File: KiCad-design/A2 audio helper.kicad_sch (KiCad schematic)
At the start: 35 parts, among them J1 PIN HEADER 1x2, J10 PIN HEADER 1x2, J11 PIN HEADER 1x3, J12 PIN HEADER 1x3, J13 PIN HEADER 1x3, J14 PIN HEADER 2x6, J2 PIN HEADER 1x2, J3 PIN HEADER 1x2, J4 SJ1-3515N, J5 PIN HEADER 1x3, J6 PIN HEADER 1x3, J7 SJ1-3515N, J8 PIN HEADER 1x5, J9 PIN HEADER 1x2, K1 SR11-5V-200-2C, SW2 SW_DPDT_x2, U1 pam8403

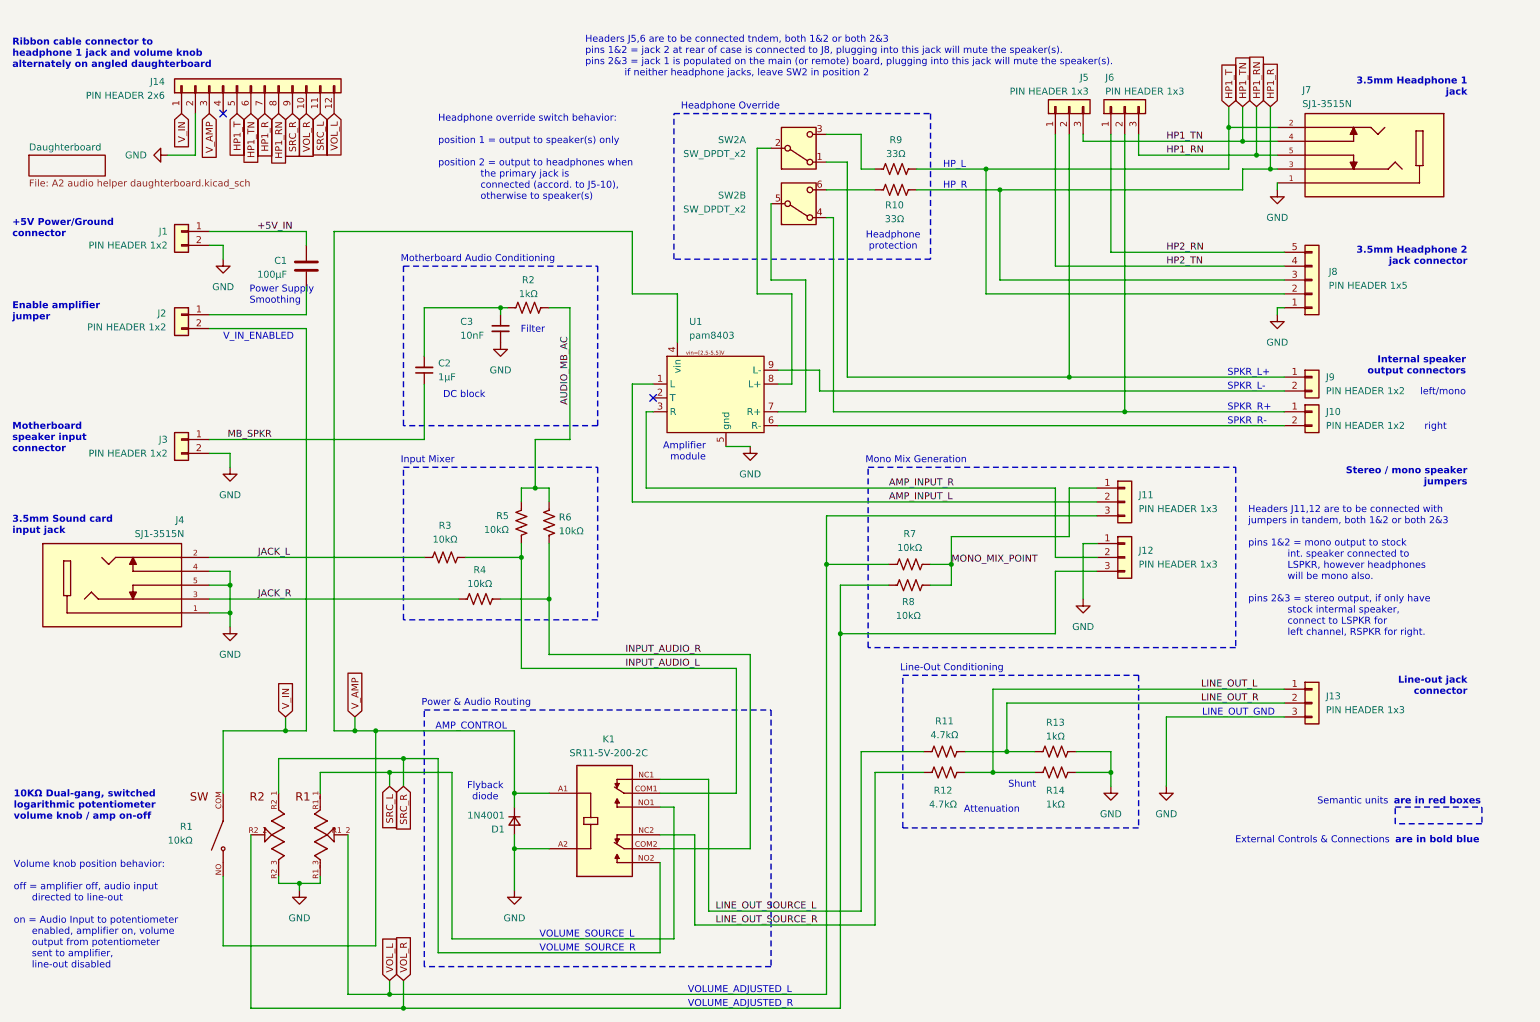
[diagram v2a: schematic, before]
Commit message: made power & speaker input connectors also horizontal
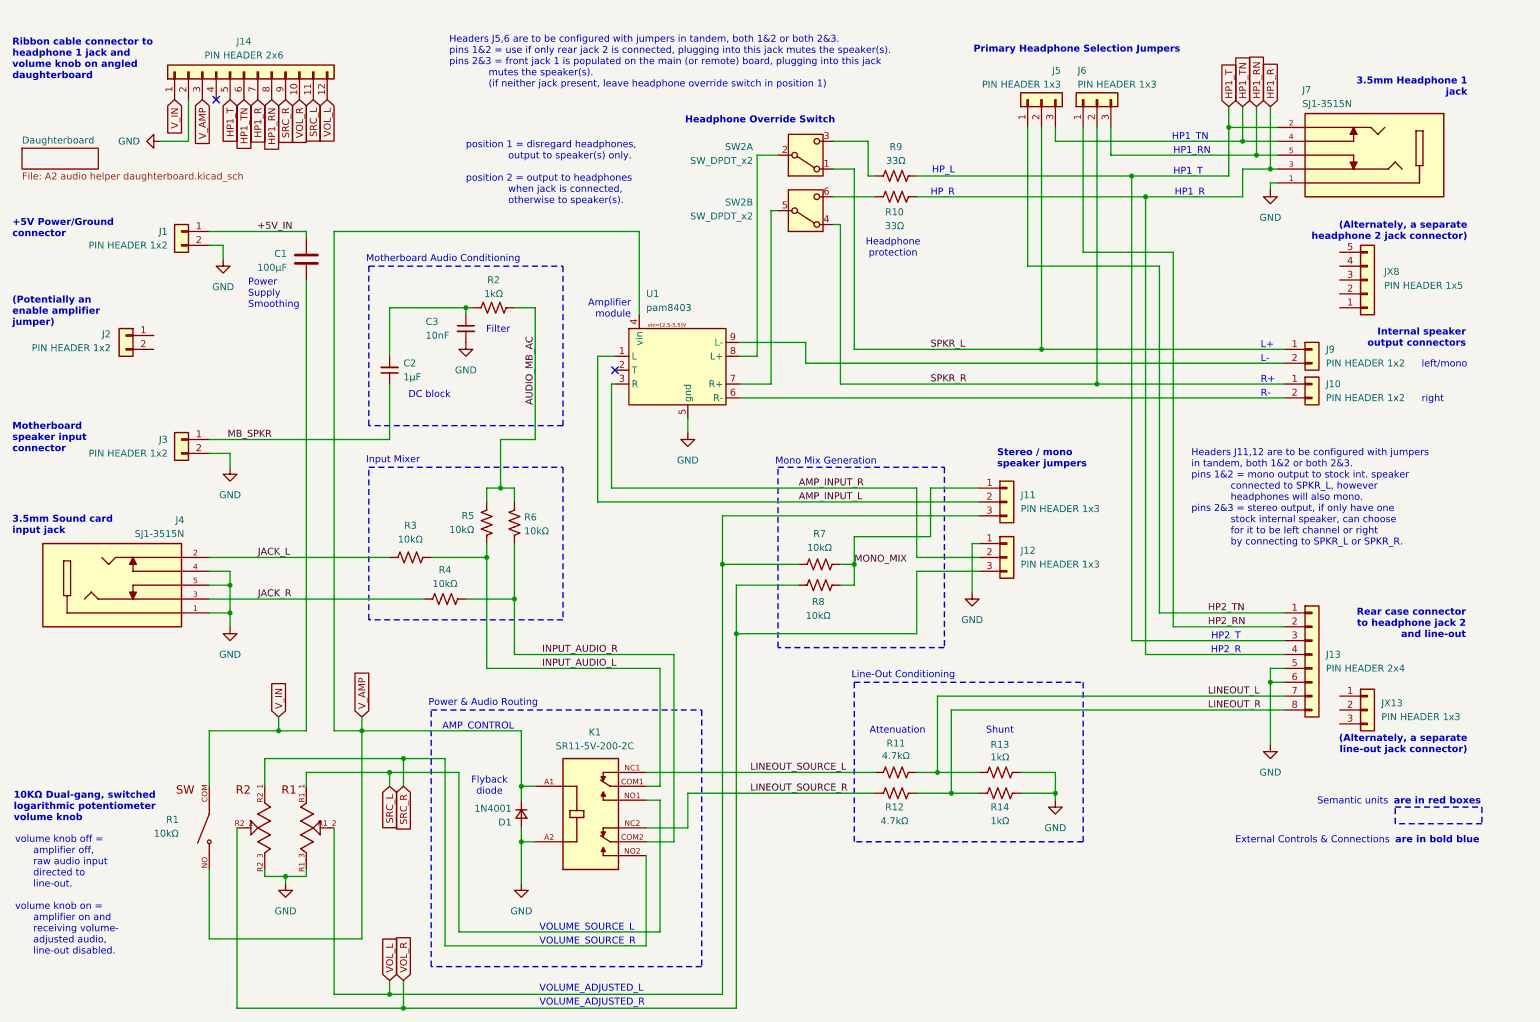
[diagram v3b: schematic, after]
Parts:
- added J13: PIN HEADER 2x4, Connector_JST:JST_PHD_B8B-PHDSS_2x04_P2.00mm_Vertical, symbol Connector_Generic:Conn_01x08
- J1: footprint Molex5267:CONN_22035025_MOL -> Molex 22-05-7025:MOLEX_22-05-7025
- J3: footprint Connector_Molex:Molex_KK-254_AE-6410-02A_1x02_P2.54mm_Vertical -> Molex 22053021:CONN_A-7478-02A_MOL
- J5, J6: footprint (none) -> Connector_PinHeader_2.54mm:PinHeader_1x03_P2.54mm_Vertical
- renumbered J13 to JX13, J8 to JX8
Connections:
- net GND: now also J13.5 (Pin_5), J13.6 (Pin_6); no longer JX13.3 (Pin_3), JX8.1 (Pin_1)
- net HP1_R: now also J13.4 (Pin_4); no longer JX8.3 (Pin_3)
- net HP1_T: now also J13.3 (Pin_3); no longer JX8.2 (Pin_2)
- net HP2_RN: now also J13.2 (Pin_2); no longer JX8.5 (Pin_5)
- net HP2_TN: now also J13.1 (Pin_1); no longer JX8.4 (Pin_4)
- net V_IN: now also C1.2; no longer J2.2 (Pin_2)
- net SPKR_L: now reaches J5.2 (Pin_2), J9.1 (Pin_1), SW2.1 (A)
- net SPKR_R: now reaches J10.1 (Pin_1), J6.2 (Pin_2), SW2.4 (A)
- net at J2.1 (Pin_1): no longer C1.2
- net LINE_OUT_L renamed LINEOUT_R
- net LINEOUT_R: now also J13.8 (Pin_8); no longer JX13.1 (Pin_1)
- net LINE_OUT_R renamed LINEOUT_L
- net LINEOUT_L: now also J13.7 (Pin_7); no longer JX13.2 (Pin_2)
- net LINE_OUT_SOURCE_L renamed LINEOUT_SOURCE_L
- net LINE_OUT_SOURCE_R renamed LINEOUT_SOURCE_R
- net MONO_MIX_POINT renamed MONO_MIX
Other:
- note added: "(Alternately, a separate headphone 2 jack connector)"
- note added: "(Alternately, a separate line-out jack connector)"
- note added: "(Potentially an enable amplifier jumper)"
- note added: "10KΩ Dual-gang, switched logarithmic potentiometer volume knob"
- note added: "HP1_R"
- note added: "HP1_RN"
- note added: "HP1_T"
- note added: "HP1_TN"
- note added: "HP2_R"
- note added: "HP2_T"
- note added: "Headers J11,12 are to be configured with jumpers in tandem, both 1&2 or both 2&3. pins 1&2 = mono output to stock int. speaker connected to SPKR_L, however headphones will also mono. pins 2&3 = stereo output, if only have one stock internal speaker, can choose for it to be left channel or right by connecting to SPKR_L or SPKR_R."
- note added: "Headers J5,6 are to be configured with jumpers in tandem, both 1&2 or both 2&3. pins 1&2 = use if only rear jack 2 is connected, plugging into this jack mutes the speaker(s). pins 2&3 = front jack 1 is populated on the main (or remote) board, plugging into this jack mutes the speaker(s). (if neither jack present, leave headphone override switch in position 1)"
- note added: "Headphone Override Switch"
- note added: "L+"
- note added: "L-"
- note added: "Primary Headphone Selection Jumpers"
- note added: "R+"
- note added: "R-"
- note added: "Rear case connector to headphone jack 2 and line-out"
- note added: "Ribbon cable connector to headphone 1 jack and volume knob on angled daughterboard"
- note added: "position 1 = disregard headphones, output to speaker(s) only. position 2 = output to headphones when jack is connected, otherwise to speaker(s)."
- note added: "volume knob off = amplifier off, raw audio input directed to line-out. volume knob on = amplifier on and receiving volume- adjusted audio, line-out disabled."
- note removed: "10KΩ Dual-gang, switched logarithmic potentiometer volume knob / amp on-off"
- note removed: "3.5mm Headphone 2 jack connector"
- note removed: "Enable amplifier jumper"
- note removed: "Headers J11,12 are to be connected with jumpers in tandem, both 1&2 or both 2&3 pins 1&2 = mono output to stock int. speaker connected to LSPKR, however headphones will be mono also. pins 2&3 = stereo output, if only have stock intermal speaker, connect to LSPKR for left channel, RSPKR for right."
- note removed: "Headers J5,6 are to be connected tndem, both 1&2 or both 2&3 pins 1&2 = jack 2 at rear of case is connected to J8, plugging into this jack will mute the speaker(s). pins 2&3 = jack 1 is populated on the main (or remote) board, plugging into this jack will mute the speaker(s). if neither headphone jacks, leave SW2 in position 2"
- note removed: "Headphone Override"
- note removed: "Headphone override switch behavior: position 1 = output to speaker(s) only position 2 = output to headphones when the primary jack is connected (accord. to J5-10), otherwise to speaker(s)"
- note removed: "LINE_OUT_GND"
- note removed: "Line-out jack connector"
- note removed: "Ribbon cable connector to headphone 1 jack and volume knob alternately on angled daughterboard"
- note removed: "SPKR_L+"
- note removed: "SPKR_L-"
- note removed: "SPKR_R+"
- note removed: "SPKR_R-"
- note removed: "V_IN_ENABLED"
- note removed: "Volume knob position behavior: off = amplifier off, audio input directed to line-out on = Audio Input to potentiometer enabled, amplifier on, volume output from potentiometer sent to amplifier, line-out disabled"
- moved on the sheet: C1, C2, C3, D1, J10, J11, J12, J14, J2, J5, J6, J9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

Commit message: added recommended decoupling cap to amp pwr/gnd
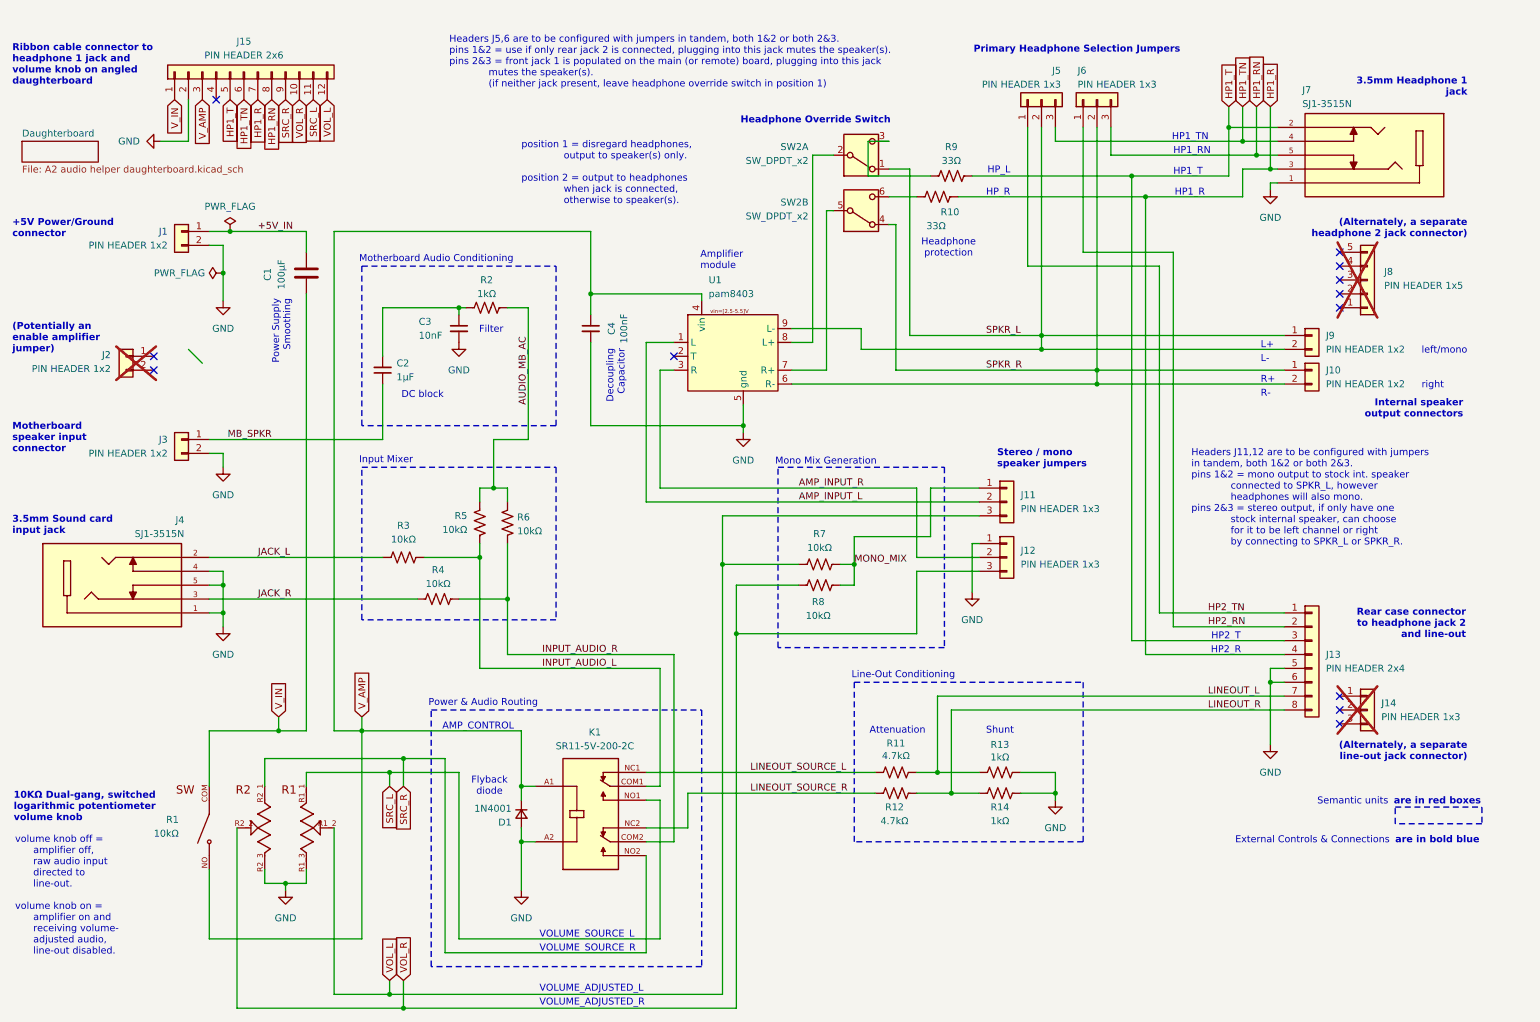
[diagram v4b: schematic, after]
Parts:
- added C4: 100nF, Capacitor_THT:C_Disc_D4.7mm_W2.5mm_P5.00mm, symbol Device:C_Small
- J14: renamed from JX13; now not fitted; now left out of the parts list
- J2: now not fitted; now left out of the parts list
- J8: renamed from JX8; now not fitted; now left out of the parts list
- renumbered J14 to J15
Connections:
- net GND: now also C4.2
- net SPKR_L: now also J9.2 (Pin_2), U1.9 (L-)
- net SPKR_R: now also J10.2 (Pin_2), U1.6 (R-)
- net V_AMP: now also C4.1
- no-connect marks 2 -> 12
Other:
- note added: "Decoupling Capacitor"
- moved on the sheet: C1, C2, C3, J10, J9, R10, R2, R3, R4, R5, R6, R9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

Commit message: changed pwr/gnd connector to more common jst connector
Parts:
- J1: footprint Molex 22-05-7025:MOLEX_22-05-7025 -> Connector_JST:JST_XH_S2B-XH-A_1x02_P2.50mm_Horizontal
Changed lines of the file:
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@@
 	(title_block
 		(title "Apple 2 Audio Helper")
-		(date "2026-02-09")
-		(rev "0.10.3")
+		(date "2026-02-18")
+		(rev "0.10.4")
 		(company "Northwest Retroventures")
 		(comment 1 "Optionally supports second internal speaker for stereo.")
@@
 			)
 		)
-		(property "Footprint" "Molex 22-05-7025:MOLEX_22-05-7025"
+		(property "Footprint" "Connector_JST:JST_XH_S2B-XH-A_1x02_P2.50mm_Horizontal"
 			(at 45.72 52.07 0)
 			(effects
